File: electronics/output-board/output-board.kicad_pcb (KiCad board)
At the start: 2 copper layers, 105.2 x 77.5 mm, 102 parts, among them J1 Conn_01x02_Male, J10 Conn_01x02_Male, J11 Conn_01x02_Male, J12 Conn_01x02_Male, J13 Conn_01x02_Male, J14 Arming switch, J15 Conn_01x02_Male, J16 Conn_01x02_Male, J17 Conn_01x02_Male, J18 Conn_01x02_Male, J19 Extra IO, J2 Conn_01x02_Male, J3 12V In, J4 Conn_01x02, J5 SWD Header, J6 Conn_01x02, J7 Conn_01x02_Male, J8 Conn_01x02_Male, J9 Conn_01x02_Male, SW1 SW_Push_Dual, U1 MAX33012EASA+, U2 LD3985M33R_SOT23, U3 STM32F446ZEHx

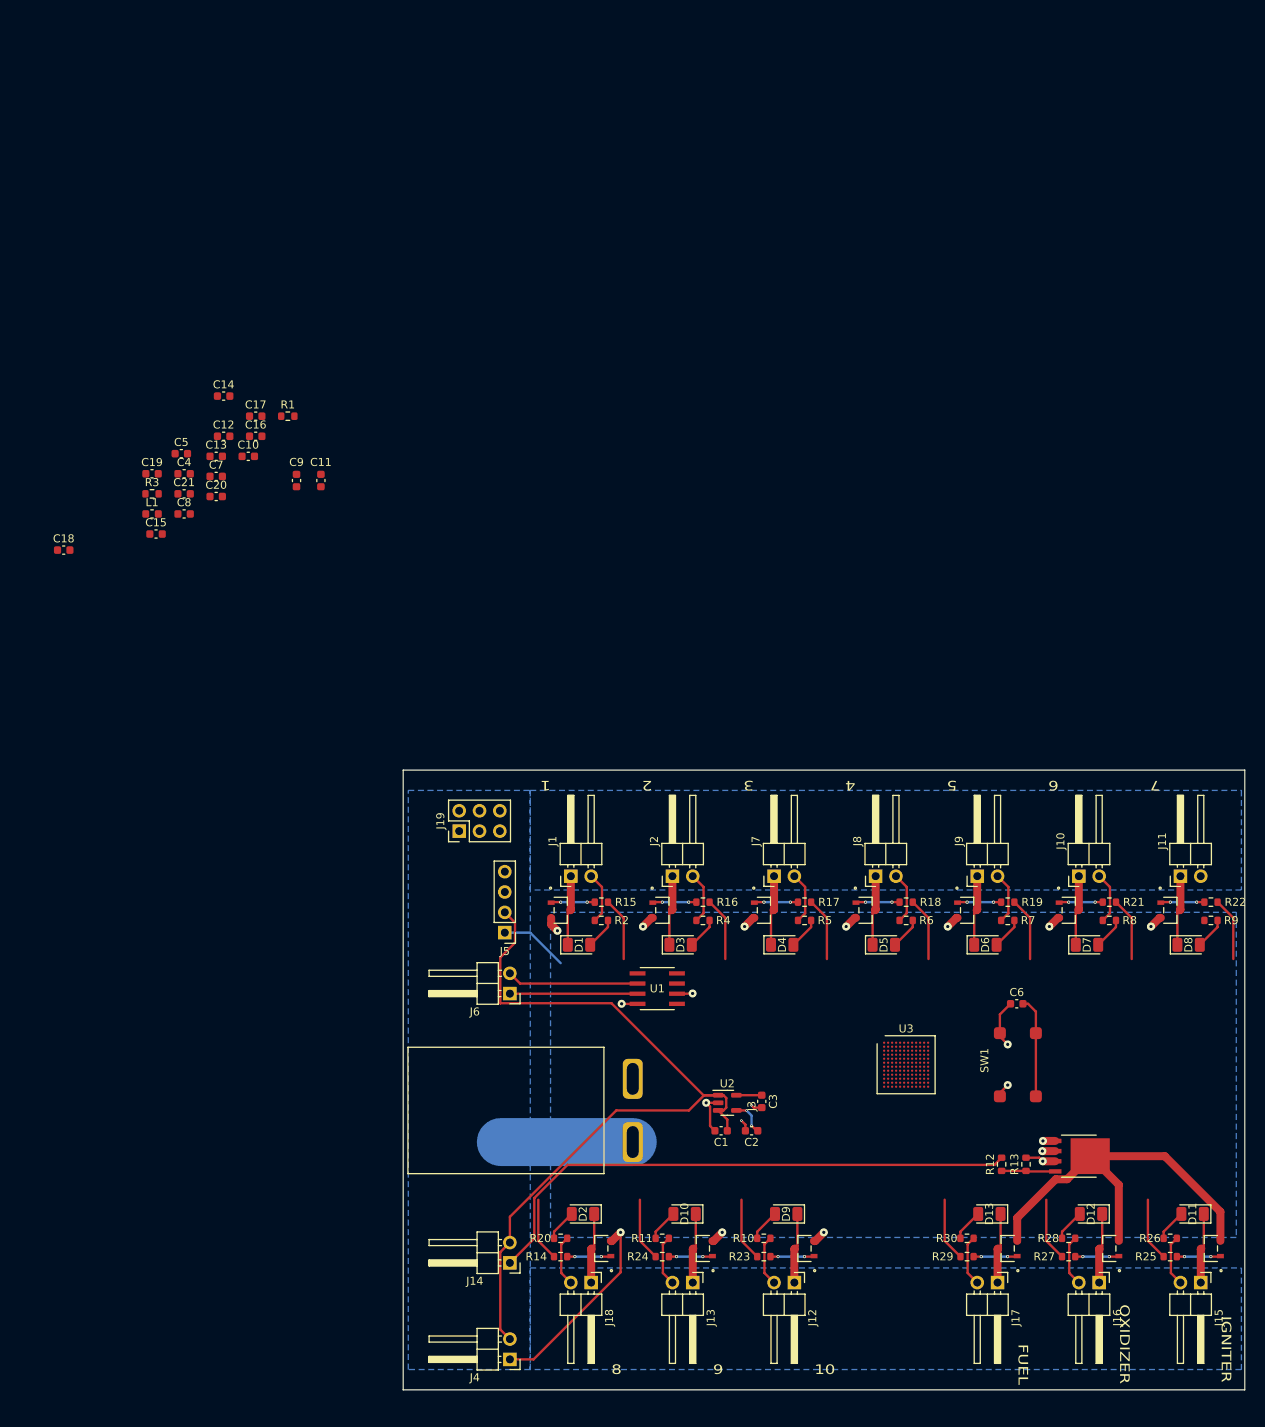
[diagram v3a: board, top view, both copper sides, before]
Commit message: Updated MCU Base and started MCU on Output Board
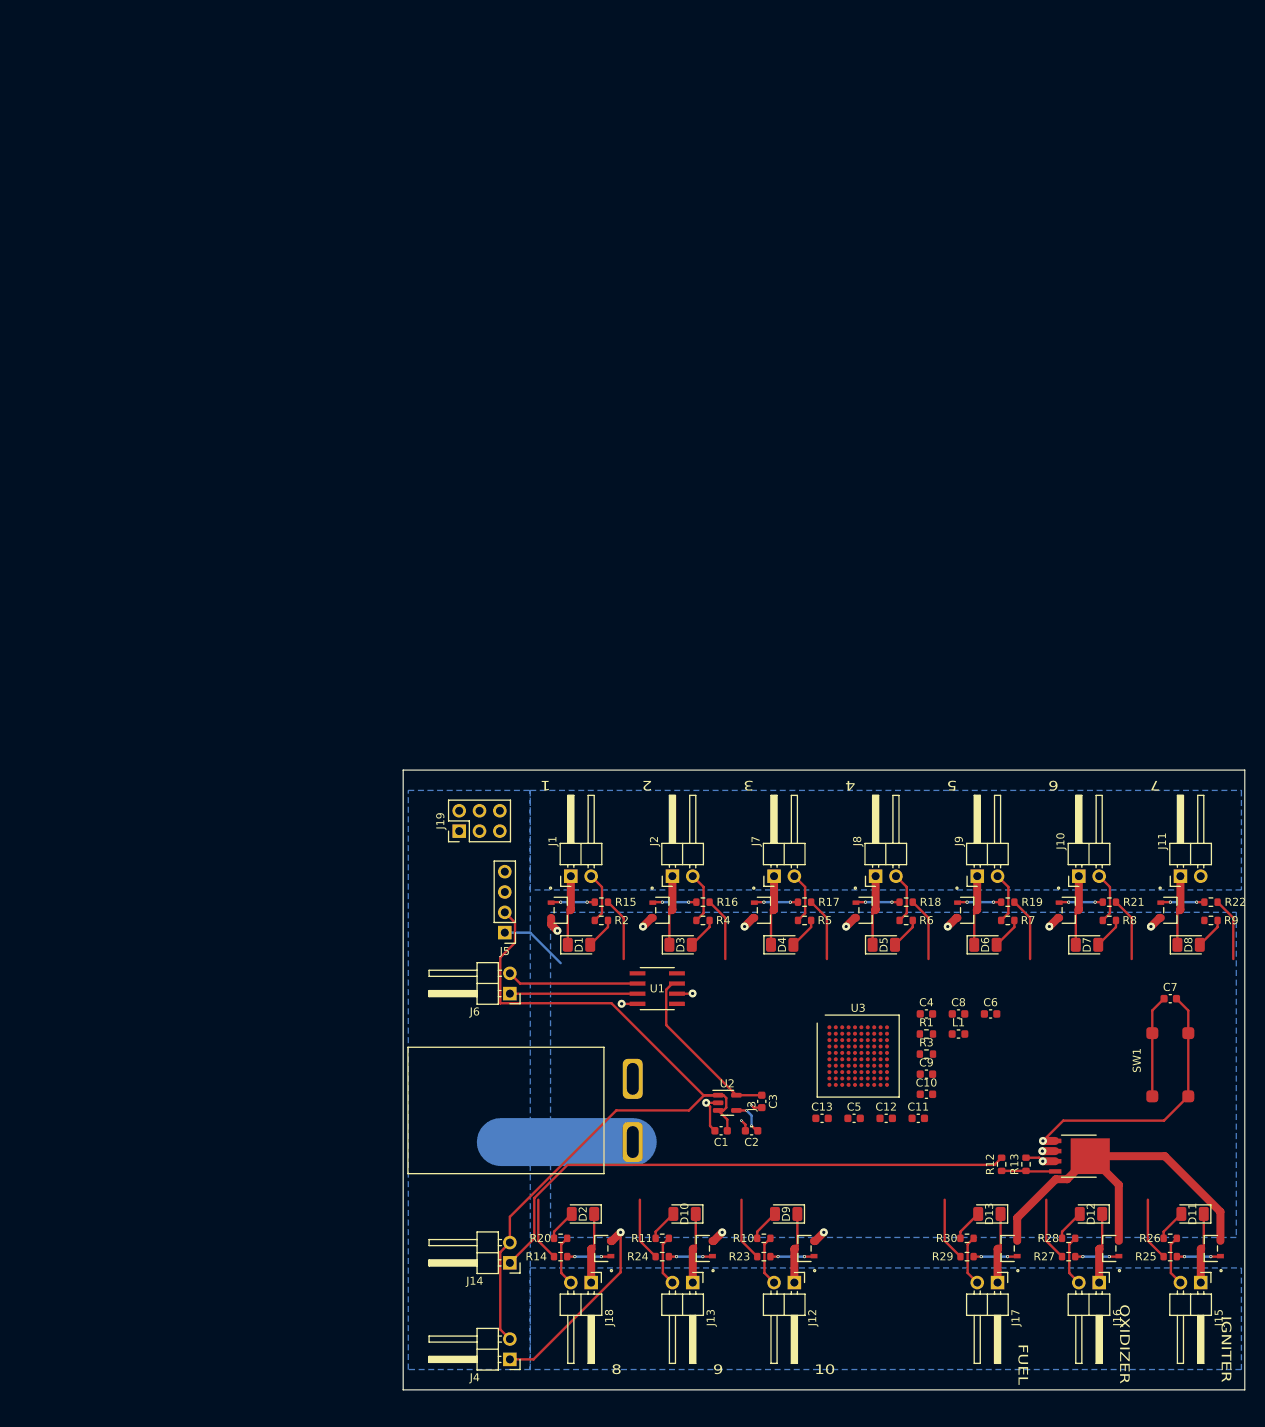
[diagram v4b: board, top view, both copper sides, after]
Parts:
- removed C14, C15, C16, C17, C18, C19, C20, C21: 100nF, Capacitor_SMD:C_0603_1608Metric
- C10, C11: value 100nF -> 20pF
- C4, C5: value 20pF -> 100nF
- C7, C8: value 2.2uF -> 100nF
- R1: value 0k -> 10k
- R3: value 10k -> 0k
- U3: value STM32F446ZEHx -> STM32F105VBH6; footprint Package_BGA:UFBGA-144_7x7mm_Layout12x12_P0.5mm -> Package_BGA:LFBGA-100_10x10mm_Layout10x10_P0.8mm
- moved C7 136.0 mm to (158.8, 125.1)
- moved L1 120.0 mm to (132.3, 129.5)
- moved R3 119.5 mm to (128.3, 132.0)
- moved C12 118.9 mm to (123.2, 140.1)
- moved C5 118.2 mm to (119.2, 140.1)
- moved C10 116.4 mm to (128.3, 137.0)
- moved C8 115.2 mm to (132.3, 127.0)
- moved C4 114.8 mm to (128.3, 127.0)
- moved C13 112.2 mm to (115.2, 140.1)
- moved R1 111.1 mm to (128.3, 129.5)
- moved C11 109.2 mm to (127.2, 140.1), turned to 0 degrees
- moved C9 108.2 mm to (128.3, 134.5), turned to 0 degrees
- moved SW1 19.1 mm to (158.8, 133.3)
- moved U3 6.09 mm to (119.7, 132.3)
- moved C6 3.51 mm to (136.3, 127.0)
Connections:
- C10 pad 1: VDDA -> GND
- C10 pad 2: GND -> Net-(C10-Pad2)
- C11 pad 1: +3V3 -> GND
- C11 pad 2: GND -> Net-(C11-Pad2)
- C4 pad 1: GND -> +3V3
- C4 pad 2: Net-(C4-Pad2) -> GND
- C5 pad 1: GND -> +3V3
- C5 pad 2: Net-(C5-Pad2) -> GND
- C6 pad 1: GND -> VDDA
- C6 pad 2: Net-(C6-Pad2) -> GND
- C8 pad 1: Net-(C8-Pad1) -> +3V3
- R1 pad 1: Net-(C4-Pad2) -> Net-(R1-Pad1)
- R1 pad 2: Net-(R1-Pad2) -> GND
- R3 pad 1: Net-(R3-Pad1) -> Net-(C11-Pad2)
- R3 pad 2: GND -> Net-(R3-Pad2)
- SW1 pad 1: GND -> Net-(C7-Pad1)
- SW1 pad 2: Net-(C6-Pad2) -> GND
- SW1 pad 3: GND -> Net-(C7-Pad1)
- SW1 pad 4: Net-(C6-Pad2) -> GND
- U3 pad A10: unconnected-(U3-PadA10) -> /SWDIO
- U3 pad A4: unconnected-(U3-PadA4) -> /MOSFET-sheet9/INPUT
- U3 pad A5: unconnected-(U3-PadA5) -> /MOSFET-sheet7/INPUT
- U3 pad A6: unconnected-(U3-PadA6) -> /MOSFET-sheet4/INPUT
- U3 pad A7: unconnected-(U3-PadA7) -> /MOSFET-sheet3/INPUT
- U3 pad A9: unconnected-(U3-PadA9) -> /SWCLK
- U3 pad B10: unconnected-(U3-PadB10) -> /CAN_TX
- U3 pad B2: unconnected-(U3-PadB2) -> +3V3
- U3 pad B4: unconnected-(U3-PadB4) -> /MOSFET-sheet8/INPUT
- U3 pad B5: unconnected-(U3-PadB5) -> /MOSFET-sheet6/INPUT
- U3 pad B8: /Ignition MOSFET/INPUT -> unconnected-(U3-PadB8)
- U3 pad C1: unconnected-(U3-PadC1) -> Net-(C10-Pad2)
- U3 pad C10: unconnected-(U3-PadC10) -> /CAN_RX
- U3 pad C2: +3V3 -> GND
- U3 pad C3: Net-(J14-Pad1) -> unconnected-(U3-PadC3)
- U3 pad C5: unconnected-(U3-PadC5) -> /MOSFET-sheet5/INPUT
- U3 pad C8: /MOSFET-sheet11/INPUT -> unconnected-(U3-PadC8)
- U3 pad D1: Net-(R1-Pad2) -> Net-(R3-Pad2)
- U3 pad D10: /CAN_TX -> unconnected-(U3-PadD10)
- U3 pad D2: GND -> +3V3
- U3 pad D3: +3V3 -> unconnected-(U3-PadD3)
- U3 pad D5: Net-(R3-Pad1) -> Net-(R1-Pad1)
- U3 pad D8: /MOSFET-sheet10/INPUT -> unconnected-(U3-PadD8)
- U3 pad E1: Net-(C5-Pad2) -> Net-(C7-Pad1)
- U3 pad E10: /CAN_RX -> unconnected-(U3-PadE10)
- U3 pad E4: unconnected-(U3-PadE4) -> GND
- U3 pad E5: +3V3 -> GND
- U3 pad E8: /MOSFET-sheet9/INPUT -> unconnected-(U3-PadE8)
- U3 pad F1: Net-(C6-Pad2) -> unconnected-(U3-PadF1)
- U3 pad F10: +3V3 -> unconnected-(U3-PadF10)
- U3 pad F8: +3V3 -> unconnected-(U3-PadF8)
- U3 pad F9: +3V3 -> unconnected-(U3-PadF9)
- U3 pad G1: unconnected-(U3-PadG1) -> GND
- U3 pad G10: GND -> unconnected-(U3-PadG10)
- U3 pad G4: GND -> unconnected-(U3-PadG4)
- U3 pad G5: +3V3 -> /MOSFET-sheet2/INPUT
- U3 pad G6: +3V3 -> unconnected-(U3-PadG6)
- U3 pad G7: +3V3 -> unconnected-(U3-PadG7)
- U3 pad G8: GND -> Net-(J14-Pad1)
- U3 pad G9: Net-(C8-Pad1) -> unconnected-(U3-PadG9)
- U3 pad H1: unconnected-(U3-PadH1) -> GND
- U3 pad H10: /MOSFET-sheet7/INPUT -> unconnected-(U3-PadH10)
- U3 pad H6: GND -> unconnected-(U3-PadH6)
- U3 pad H7: Net-(C7-Pad1) -> unconnected-(U3-PadH7)
- U3 pad J1: GND -> VDDA
- U3 pad J10: /MOSFET-sheet4/INPUT -> unconnected-(U3-PadJ10)
- U3 pad J4: unconnected-(U3-PadJ4) -> /MOSFET-sheet/INPUT
- U3 pad J6: /MOSFET-sheet1/INPUT -> unconnected-(U3-PadJ6)
- U3 pad J7: unconnected-(U3-PadJ7) -> /MOSFET-sheet10/INPUT
- U3 pad K1: GND -> VDDA
- U3 pad K4: unconnected-(U3-PadK4) -> /MOSFET-sheet1/INPUT
- U3 pad K6: /MOSFET-sheet/INPUT -> unconnected-(U3-PadK6)
- U3 pad K7: unconnected-(U3-PadK7) -> /MOSFET-sheet11/INPUT
- U3 pad K8: unconnected-(U3-PadK8) -> /Ignition MOSFET/INPUT
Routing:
- net GND: track 76.0 -> 101.5 mm, vias 20 -> 18
- net +3V3: track 3.17 -> 21.7 mm
- net Net-(C7-Pad1): track 0.00 -> 12.8 mm
- net Net-(C6-Pad2): track 12.6 -> 0.00 mm

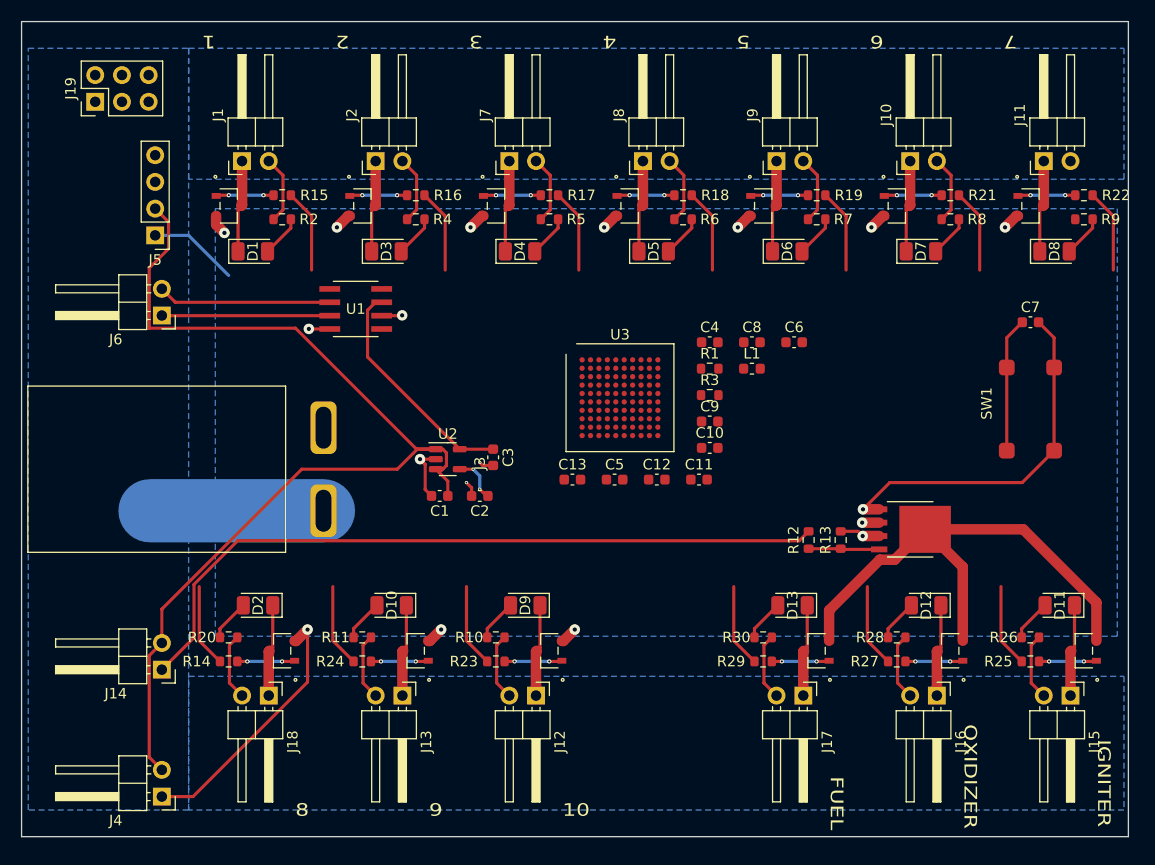
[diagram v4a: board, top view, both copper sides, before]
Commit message: Continued Laying Out Output Board
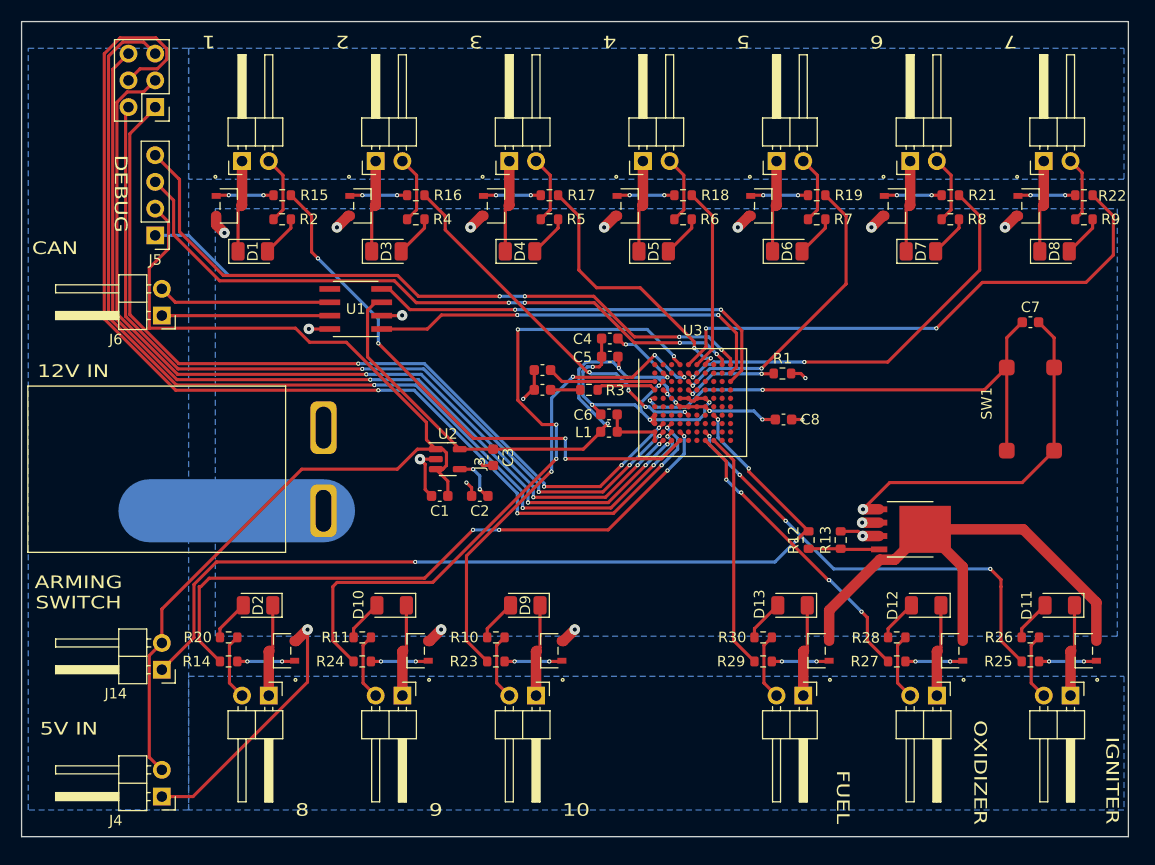
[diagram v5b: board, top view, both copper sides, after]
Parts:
- removed C12, C13, C9: 100nF, Capacitor_SMD:C_0603_1608Metric
- moved C6 18.9 mm to (118.7, 133.9), turned to 180 degrees
- moved C10 17.5 mm to (112.4, 129.6)
- moved C11 17.2 mm to (112.4, 131.5)
- moved L1 14.9 mm to (118.7, 135.5), turned to 180 degrees
- moved C5 11.7 mm to (118.8, 128.4), turned to 180 degrees
- moved R3 11.5 mm to (116.8, 131.5)
- moved C4 9.51 mm to (118.8, 126.6), turned to 180 degrees
- moved C8 7.93 mm to (135.3, 134.3)
- moved U3 6.92 mm to (126.6, 132.7)
- moved R1 6.92 mm to (135.2, 130.0)
- moved J19 5.72 mm to (75.6, 104.6), turned to 180 degrees
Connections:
- J19 pad 1: unconnected-(J19-Pad1) -> Net-(U3-PadH2)
- J19 pad 2: unconnected-(J19-Pad2) -> Net-(U3-PadJ2)
- J19 pad 3: unconnected-(J19-Pad3) -> Net-(U3-PadK2)
- J19 pad 4: unconnected-(J19-Pad4) -> Net-(U3-PadH3)
- J19 pad 5: unconnected-(J19-Pad5) -> Net-(U3-PadJ3)
- J19 pad 6: unconnected-(J19-Pad6) -> Net-(U3-PadK3)
- U3 pad H2: unconnected-(U3-PadH2) -> Net-(U3-PadH2)
- U3 pad H3: unconnected-(U3-PadH3) -> Net-(U3-PadH3)
- U3 pad J2: unconnected-(U3-PadJ2) -> Net-(U3-PadJ2)
- U3 pad J3: unconnected-(U3-PadJ3) -> Net-(U3-PadJ3)
- U3 pad K2: unconnected-(U3-PadK2) -> Net-(U3-PadK2)
- U3 pad K3: unconnected-(U3-PadK3) -> Net-(U3-PadK3)
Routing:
- net Net-(U3-PadH3): track 0.00 -> 106.5 mm, vias 0 -> 4
- net Net-(U3-PadJ3): track 0.00 -> 96.4 mm, vias 0 -> 4
- net Net-(U3-PadK3): track 0.00 -> 89.2 mm, vias 0 -> 4
- net Net-(U3-PadK2): track 0.00 -> 86.6 mm, vias 0 -> 4
- net Net-(U3-PadH2): track 0.00 -> 80.9 mm, vias 0 -> 4
- net Net-(U3-PadJ2): track 0.00 -> 80.8 mm, vias 0 -> 4
- net /SWDIO: track 0.00 -> 66.2 mm, vias 0 -> 4
- net /SWCLK: track 0.00 -> 63.3 mm, vias 0 -> 4
- net /MOSFET-sheet9/INPUT: track 7.93 -> 65.7 mm, vias 0 -> 4
- net /MOSFET-sheet/INPUT: track 7.93 -> 61.5 mm, vias 0 -> 4
- net +3V3: track 21.7 -> 71.2 mm, vias 0 -> 8
- net /MOSFET-sheet1/INPUT: track 7.93 -> 52.6 mm, vias 0 -> 4
- net /MOSFET-sheet7/INPUT: track 7.93 -> 52.2 mm, vias 0 -> 2
- net /CAN_RX: track 0.00 -> 41.2 mm, vias 0 -> 2
- net /CAN_TX: track 0.00 -> 39.0 mm, vias 0 -> 2
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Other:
- board text added: "12V IN"
- board text added: "5V IN"
- board text added: "ARMING SWITCH"
- board text added: "CAN"
- board text added: "DEBUG"
